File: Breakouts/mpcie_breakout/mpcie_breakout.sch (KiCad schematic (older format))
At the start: 28 parts, among them J1 9-39, J10 8-14,G, J2 1-9, J3 40-48,43-51, J4 PWR, J5 16-34, J6 USB, J7 SIM_Card, J8 USB_OTG, J9 APWR, U1 MPCIE-Socket

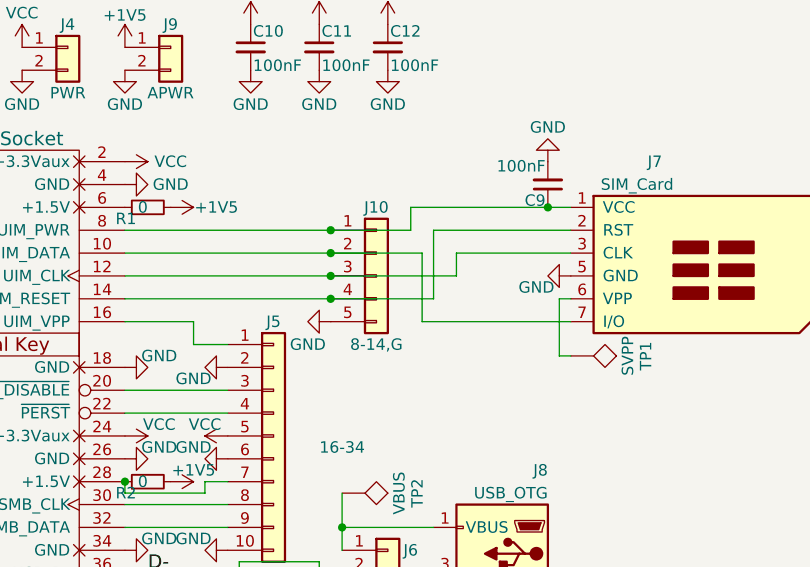
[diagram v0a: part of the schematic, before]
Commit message: Adding SIM net labels to mPCI-E breakout - SIM slot not fixed yet
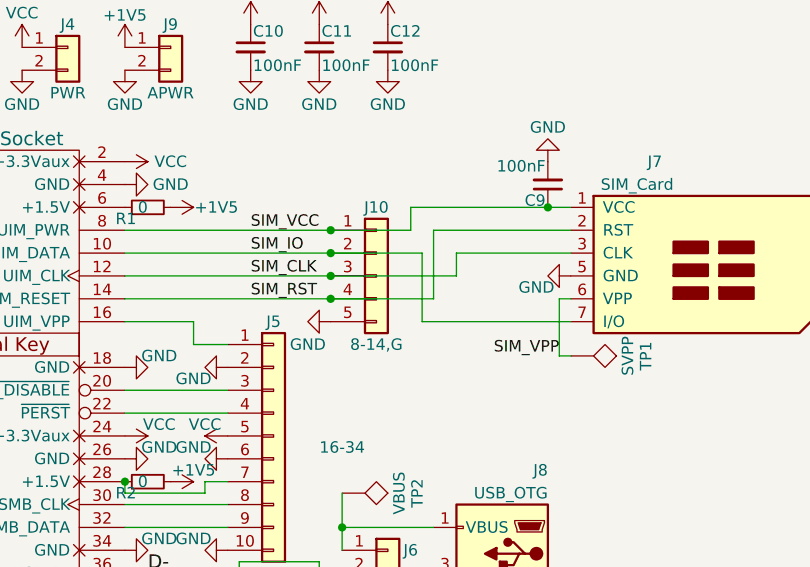
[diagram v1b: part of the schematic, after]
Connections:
- net SIM_IO: now reaches J10.2 (Pin_2), J7.7 (I/O), U1.10 (UIM_DATA)
- net SIM_CLK: now reaches J10.3 (Pin_3), J7.3 (CLK), U1.12 (UIM_CLK)
- net SIM_RST: now reaches J10.4 (Pin_4), J7.2 (RST), U1.14 (UIM_RESET)
- net SIM_VCC: now reaches C9.1, J10.1 (Pin_1), J7.1 (VCC), U1.8 (UIM_PWR)
- net SIM_VPP: now reaches J7.6 (VPP), TP1.1
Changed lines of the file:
@@
 Wire Wire Line
 	6150 2900 6600 2900
+Text Label 5800 2600 0    50   ~ 0
+SIM_VCC
+Text Label 5800 2700 0    50   ~ 0
+SIM_IO
+Text Label 5800 2800 0    50   ~ 0
+SIM_CLK
+Text Label 5800 2900 0    50   ~ 0
+SIM_RST
+Text Label 7150 3150 2    50   ~ 0
+SIM_VPP
 $EndSCHEMATC

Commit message: Adding v2 of the mPCIe breakout with a README
Changelog in README
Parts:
- added C13, C14: 100nF, Capacitor_SMD:C_0805_2012Metric, symbol Device:C_Small
- added U2: AP1117-33, Package_TO_SOT_SMD:SOT-223-3_TabPin2, symbol Regulator_Linear:AP1117-33
- added U3: AP1117-15, Package_TO_SOT_SMD:SOT-223-3_TabPin2, symbol Regulator_Linear:AP1117-15
- C1, C10, C11, C12, C2, C3, C4, C5, C6, C7, C8, C9: footprint Capacitors_SMD:C_0805 -> Capacitor_SMD:C_0805_2012Metric
- J1: symbol conn:Conn_01x16 -> mpcie_breakout-rescue:Conn_01x16-conn
- J10, J2, J6: symbol conn:Conn_01x05 -> mpcie_breakout-rescue:Conn_01x05-conn
- J3: symbol conn:Conn_02x05_Counter_Clockwise -> mpcie_breakout-rescue:Conn_02x05_Counter_Clockwise-conn
- J4, J9: symbol conn:Conn_01x02 -> mpcie_breakout-rescue:Conn_01x02-conn
- J5: symbol conn:Conn_01x10 -> mpcie_breakout-rescue:Conn_01x10-conn
- J7: symbol conn:SIM_Card -> mpcie_breakout-rescue:SIM_Card-conn
- J8: symbol conn:USB_OTG -> mpcie_breakout-rescue:USB_OTG-conn
- R1, R2, R3: footprint Resistors_SMD:R_0402 -> Resistor_SMD:R_0603_1608Metric_Pad1.05x0.95mm_HandSolder
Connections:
- net +1V5: now also U3.2 (VO)
- net GND: now also J7.C5 (GND), C13.2, C14.2, U2.1 (GND), U3.1 (GND); no longer J7.5 (GND)
- net SIM_CLK: now also J7.C3 (CLK); no longer J7.3 (CLK)
- net SIM_IO: now also J7.C7 (I/O); no longer J7.7 (I/O)
- net SIM_RST: now also J7.C2 (RST); no longer J7.2 (RST)
- net SIM_VCC: now also J7.C1 (VCC); no longer J7.1 (VCC)
- net SIM_VPP: now also J7.C6 (VPP); no longer J7.6 (VPP)
- net VCC: now also C13.1, U2.2 (VO)
- net VBUS: now reaches J6.1 (Pin_1), J8.1 (VBUS), TP2.1
- net VBUS: now also C14.1, U2.3 (VI), U3.3 (VI)
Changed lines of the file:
@@
 EESchema Schematic File Version 4
-LIBS:mpcie_breakout-cache
-EELAYER 29 0
+EELAYER 30 0
 EELAYER END
 $Descr A4 11693 8268
@@
 $EndComp
 $Comp
-L conn:SIM_Card J7
+L mpcie_breakout-rescue:SIM_Card-conn J7
 U 1 1 5CC07ACA
 P 7700 2800
@@
 $EndComp
 $Comp
-L conn:USB_OTG J8
+L mpcie_breakout-rescue:USB_OTG-conn J8
 U 1 1 5CC07C94
 P 6900 4100
@@
 F 0 "R1" V 5300 2550 50  0000 L CNN
 F 1 "0" V 5350 2500 50  0000 L CNN
-F 2 "Resistors_SMD:R_0402" H 5350 2500 50  0001 C CNN
+F 2 "Resistor_SMD:R_0603_1608Metric_Pad1.05x0.95mm_HandSolder" H 5350 2500 50  0001 C CNN
 F 3 "" H 5350 2500 50  0001 C CNN
 	1    5350 2500
@@
 F 0 "R3" V 5300 4750 50  0000 L CNN
 F 1 "0" V 5350 4700 50  0000 L CNN
-F 2 "Resistors_SMD:R_0402" H 5350 4700 50  0001 C CNN
+F 2 "Resistor_SMD:R_0603_1608Metric_Pad1.05x0.95mm_HandSolder" H 5350 4700 50  0001 C CNN
 F 3 "" H 5350 4700 50  0001 C CNN
 	1    5350 4700
@@
 $EndComp
 $Comp
-L conn:Conn_02x05_Counter_Clockwise J3
+L mpcie_breakout-rescue:Conn_02x05_Counter_Clockwise-conn J3
 U 1 1 5CC08111
 P 4600 5300
@@
 $EndComp
 $Comp
-L conn:Conn_01x05 J6
+L mpcie_breakout-rescue:Conn_01x05-conn J6
 U 1 1 5CC084A6
 P 6400 4200
@@
 $EndComp
 $Comp
-L conn:Conn_01x05 J2
+L mpcie_breakout-rescue:Conn_01x05-conn J2
 U 1 1 5CC08647
 P 3450 2500
@@
 $EndComp
 $Comp
-L conn:Conn_01x02 J4
+L mpcie_breakout-rescue:Conn_01x02-conn J4
 U 1 1 5CC088EB
 P 5000 1800
@@
 F 0 "R2" V 5300 3750 50  0000 L CNN
 F 1 "0" V 5350 3700 50  0000 L CNN
-F 2 "Resistors_SMD:R_0402" H 5350 3700 50  0001 C CNN
+F 2 "Resistor_SMD:R_0603_1608Metric_Pad1.05x0.95mm_HandSolder" H 5350 3700 50  0001 C CNN
 F 3 "" H 5350 3700 50  0001 C CNN
 	1    5350 3700
@@
 F 0 "C7" H 4010 1870 50  0000 L CNN
 F 1 "100nF" H 4010 1720 50  0000 L CNN
-F 2 "Capacitors_SMD:C_0805" H 4000 1800 50  0001 C CNN
+F 2 "Capacitor_SMD:C_0805_2012Metric" H 4000 1800 50  0001 C CNN
 F 3 "" H 4000 1800 50  0001 C CNN
 	1    4000 1800
@@
 F 0 "C8" H 4310 1870 50  0000 L CNN
 F 1 "100nF" H 4310 1720 50  0000 L CNN
-F 2 "Capacitors_SMD:C_0805" H 4300 1800 50  0001 C CNN
+F 2 "Capacitor_SMD:C_0805_2012Metric" H 4300 1800 50  0001 C CNN
 F 3 "" H 4300 1800 50  0001 C CNN
 	1    4300 1800
@@
 F 0 "C6" H 3710 1870 50  0000 L CNN
 F 1 "100nF" H 3710 1720 50  0000 L CNN
-F 2 "Capacitors_SMD:C_0805" H 3700 1800 50  0001 C CNN
+F 2 "Capacitor_SMD:C_0805_2012Metric" H 3700 1800 50  0001 C CNN
 F 3 "" H 3700 1800 50  0001 C CNN
 	1    3700 1800
@@
 F 0 "C5" H 3410 1870 50  0000 L CNN
 F 1 "100nF" H 3410 1720 50  0000 L CNN
-F 2 "Capacitors_SMD:C_0805" H 3400 1800 50  0001 C CNN
+F 2 "Capacitor_SMD:C_0805_2012Metric" H 3400 1800 50  0001 C CNN
 F 3 "" H 3400 1800 50  0001 C CNN
 	1    3400 1800
@@
 $EndComp
 $Comp
-L conn:Conn_01x16 J1
+L mpcie_breakout-rescue:Conn_01x16-conn J1
 U 1 1 5CC09A5E
 P 3100 3500
@@
 $EndComp
 $Comp
-L conn:Conn_01x10 J5
+L mpcie_breakout-rescue:Conn_01x10-conn J5
 U 1 1 5CC09F73
 P 5900 3500
 F 0 "J5" H 5900 4000 50  0000 C CNN
-F 1 "16-34" H 6200 3450 50  0000 C CNN
+F 1 "16-34" H 6100 3650 50  0000 C CNN
 F 2 "Pin_Headers:Pin_Header_Straight_2x05_Pitch2.54mm" H 5900 3500 50  0001 C CNN
 F 3 "" H 5900 3500 50  0001 C CNN
@@
 F 0 "C3" H 2860 1870 50  0000 L CNN
 F 1 "100nF" H 2860 1720 50  0000 L CNN
-F 2 "Capacitors_SMD:C_0805" H 2850 1800 50  0001 C CNN
+F 2 "Capacitor_SMD:C_0805_2012Metric" H 2850 1800 50  0001 C CNN
 F 3 "" H 2850 1800 50  0001 C CNN
 	1    2850 1800
@@
 F 0 "C4" H 3160 1870 50  0000 L CNN
 F 1 "100nF" H 3160 1720 50  0000 L CNN
-F 2 "Capacitors_SMD:C_0805" H 3150 1800 50  0001 C CNN
+F 2 "Capacitor_SMD:C_0805_2012Metric" H 3150 1800 50  0001 C CNN
 F 3 "" H 3150 1800 50  0001 C CNN
 	1    3150 1800
@@
 F 0 "C2" H 2560 1870 50  0000 L CNN
 F 1 "100nF" H 2560 1720 50  0000 L CNN
-F 2 "Capacitors_SMD:C_0805" H 2550 1800 50  0001 C CNN
+F 2 "Capacitor_SMD:C_0805_2012Metric" H 2550 1800 50  0001 C CNN
 F 3 "" H 2550 1800 50  0001 C CNN
 	1    2550 1800
@@
 F 0 "C1" H 2260 1870 50  0000 L CNN
 F 1 "100nF" H 2260 1720 50  0000 L CNN
-F 2 "Capacitors_SMD:C_0805" H 2250 1800 50  0001 C CNN
+F 2 "Capacitor_SMD:C_0805_2012Metric" H 2250 1800 50  0001 C CNN
 F 3 "" H 2250 1800 50  0001 C CNN
 	1    2250 1800
@@
 F 0 "C9" H 7110 2470 50  0000 L CNN
 F 1 "100nF" H 7110 2320 50  0000 L CNN
-F 2 "Capacitors_SMD:C_0805" H 7100 2400 50  0001 C CNN
+F 2 "Capacitor_SMD:C_0805_2012Metric" H 7100 2400 50  0001 C CNN
 F 3 "" H 7100 2400 50  0001 C CNN
 	1    7100 2400
@@
 $EndComp
 $Comp
-L conn:Conn_01x02 J9
+L mpcie_breakout-rescue:Conn_01x02-conn J9
 U 1 1 5CC0945A
 P 5450 1800
@@
 	6700 2800 6700 2700
 $Comp
-L conn:Conn_01x05 J10
+L mpcie_breakout-rescue:Conn_01x05-conn J10
 U 1 1 5CC0A195
 P 6350 2800
@@
 F 0 "C10" H 5810 1870 50  0000 L CNN
 F 1 "100nF" H 5810 1720 50  0000 L CNN
-F 2 "Capacitors_SMD:C_0805" H 5800 1800 50  0001 C CNN
+F 2 "Capacitor_SMD:C_0805_2012Metric" H 5800 1800 50  0001 C CNN
 F 3 "" H 5800 1800 50  0001 C CNN
 	1    5800 1800
@@
 F 0 "C11" H 6110 1870 50  0000 L CNN
 F 1 "100nF" H 6110 1720 50  0000 L CNN
-F 2 "Capacitors_SMD:C_0805" H 6100 1800 50  0001 C CNN
+F 2 "Capacitor_SMD:C_0805_2012Metric" H 6100 1800 50  0001 C CNN
 F 3 "" H 6100 1800 50  0001 C CNN
 	1    6100 1800
@@
 F 0 "C12" H 6410 1870 50  0000 L CNN
 F 1 "100nF" H 6410 1720 50  0000 L CNN
-F 2 "Capacitors_SMD:C_0805" H 6400 1800 50  0001 C CNN
+F 2 "Capacitor_SMD:C_0805_2012Metric" H 6400 1800 50  0001 C CNN
 F 3 "" H 6400 1800 50  0001 C CNN
 	1    6400 1800
@@
 Text Label 7150 3150 2    50   ~ 0
 SIM_VPP
+$Comp
+L Regulator_Linear:AP1117-33 U2
+U 1 1 5FF64EDB
+P 1300 3000
+F 0 "U2" H 1300 3242 50  0000 C CNN
+F 1 "AP1117-33" H 1300 3151 50  0000 C CNN
+F 2 "Package_TO_SOT_SMD:SOT-223-3_TabPin2" H 1300 3200 50  0001 C CNN
+F 3 "http://www.diodes.com/datasheets/AP1117.pdf" H 1400 2750 50  0001 C CNN
+	1    1300 3000
+	1    0    0    -1
+$EndComp
+$Comp
+L power:VBUS #PWR0101
+U 1 1 5FF67FCA
+P 6200 3750
+F 0 "#PWR0101" H 6200 3600 50  0001 C CNN
+F 1 "VBUS" H 6215 3923 50  0000 C CNN
+F 2 "" H 6200 3750 50  0001 C CNN
+F 3 "" H 6200 3750 50  0001 C CNN
+	1    6200 3750
+	1    0    0    -1
+$EndComp
+Connection ~ 6200 3750
+$Comp
+L power:VBUS #PWR0102
+U 1 1 5FF68DFF
+P 1000 3000
+F 0 "#PWR0102" H 1000 2850 50  0001 C CNN
+F 1 "VBUS" H 900 3150 50  0000 C CNN
+F 2 "" H 1000 3000 50  0001 C CNN
+F 3 "" H 1000 3000 50  0001 C CNN
+	1    1000 3000
+	1    0    0    -1
+$EndComp
+$Comp
+L power:VCC #PWR0103
+U 1 1 5FF6C4C8
+P 1600 3000
+F 0 "#PWR0103" H 1600 2850 50  0001 C CNN
+F 1 "VCC" H 1650 3150 50  0000 C CNN
+F 2 "" H 1600 3000 50  0001 C CNN
+F 3 "" H 1600 3000 50  0001 C CNN
+	1    1600 3000
+	1    0    0    -1
+$EndComp
+$Comp
+L power:GND #PWR0104
+U 1 1 5FF6E995
+P 1300 3300
+F 0 "#PWR0104" H 1300 3050 50  0001 C CNN
+F 1 "GND" H 1300 3150 50  0000 C CNN
+F 2 "" H 1300 3300 50  0001 C CNN
+F 3 "" H 1300 3300 50  0001 C CNN
+	1    1300 3300
+	1    0    0    -1
+$EndComp
+$Comp
+L Regulator_Linear:AP1117-15 U3
+U 1 1 5FF703B3
+P 1300 4100
+F 0 "U3" H 1300 4342 50  0000 C CNN
+F 1 "AP1117-15" H 1300 4251 50  0000 C CNN
+F 2 "Package_TO_SOT_SMD:SOT-223-3_TabPin2" H 1300 4300 50  0001 C CNN
+F 3 "http://www.diodes.com/datasheets/AP1117.pdf" H 1400 3850 50  0001 C CNN
+	1    1300 4100
+	1    0    0    -1
+$EndComp
+$Comp
+L power:VBUS #PWR0105
+U 1 1 5FF71952
+P 1000 4100
+F 0 "#PWR0105" H 1000 3950 50  0001 C CNN
+F 1 "VBUS" H 900 4250 50  0000 C CNN
+F 2 "" H 1000 4100 50  0001 C CNN
+F 3 "" H 1000 4100 50  0001 C CNN
+	1    1000 4100
+	1    0    0    -1
+$EndComp
+$Comp
+L power:+1V5 #PWR0106
+U 1 1 5FF721B1
+P 1600 4100
+F 0 "#PWR0106" H 1600 3950 50  0001 C CNN
+F 1 "+1V5" H 1600 4240 50  0000 C CNN
+F 2 "" H 1600 4100 50  0001 C CNN
+F 3 "" H 1600 4100 50  0001 C CNN
+	1    1600 4100
+	1    0    0    -1
+$EndComp
+$Comp
+L power:GND #PWR0107
+U 1 1 5FF729DE
+P 1300 4400
+F 0 "#PWR0107" H 1300 4150 50  0001 C CNN
+F 1 "GND" H 1300 4250 50  0000 C CNN
+F 2 "" H 1300 4400 50  0001 C CNN
+F 3 "" H 1300 4400 50  0001 C CNN
+	1    1300 4400
+	1    0    0    -1
+$EndComp
+$Comp
+L Device:C_Small C14
+U 1 1 5FF98EFD
+P 1450 5250
+F 0 "C14" H 1460 5320 50  0000 L CNN
+F 1 "100nF" H 1460 5170 50  0000 L CNN
+F 2 "Capacitor_SMD:C_0805_2012Metric" H 1450 5250 50  0001 C CNN
+F 3 "" H 1450 5250 50  0001 C CNN
+	1    1450 5250
+	1    0    0    -1
+$EndComp
+$Comp
+L Device:C_Small C13
+U 1 1 5FF98F03
+P 1150 5250
+F 0 "C13" H 1160 5320 50  0000 L CNN
+F 1 "100nF" H 1160 5170 50  0000 L CNN
+F 2 "Capacitor_SMD:C_0805_2012Metric" H 1150 5250 50  0001 C CNN
+F 3 "" H 1150 5250 50  0001 C CNN
+	1    1150 5250
+	1    0    0    -1
+$EndComp
+$Comp
+L power:VCC #PWR0108
+U 1 1 5FF98F09
+P 1150 5150
+F 0 "#PWR0108" H 1150 5000 50  0001 C CNN
+F 1 "VCC" H 1150 5300 50  0000 C CNN
+F 2 "" H 1150 5150 50  0001 C CNN
+F 3 "" H 1150 5150 50  0001 C CNN
+	1    1150 5150
+	1    0    0    -1
+$EndComp
+$Comp
+L power:GND #PWR0109
+U 1 1 5FF98F21
+P 1150 5350
+F 0 "#PWR0109" H 1150 5100 50  0001 C CNN
+F 1 "GND" H 1150 5200 50  0000 C CNN
+F 2 "" H 1150 5350 50  0001 C CNN
+F 3 "" H 1150 5350 50  0001 C CNN
+	1    1150 5350
+	1    0    0    -1
+$EndComp
+$Comp
+L power:GND #PWR0110
+U 1 1 5FF98F27
+P 1450 5350
+F 0 "#PWR0110" H 1450 5100 50  0001 C CNN
+F 1 "GND" H 1450 5200 50  0000 C CNN
+F 2 "" H 1450 5350 50  0001 C CNN
+F 3 "" H 1450 5350 50  0001 C CNN
+	1    1450 5350
+	1    0    0    -1
+$EndComp
+$Comp
+L power:VBUS #PWR0115
+U 1 1 5FF9F3D9
+P 1450 5150
+F 0 "#PWR0115" H 1450 5000 50  0001 C CNN
+F 1 "VBUS" H 1350 5300 50  0000 C CNN
+F 2 "" H 1450 5150 50  0001 C CNN
+F 3 "" H 1450 5150 50  0001 C CNN
+	1    1450 5150
+	1    0    0    -1
+$EndComp
 $EndSCHEMATC

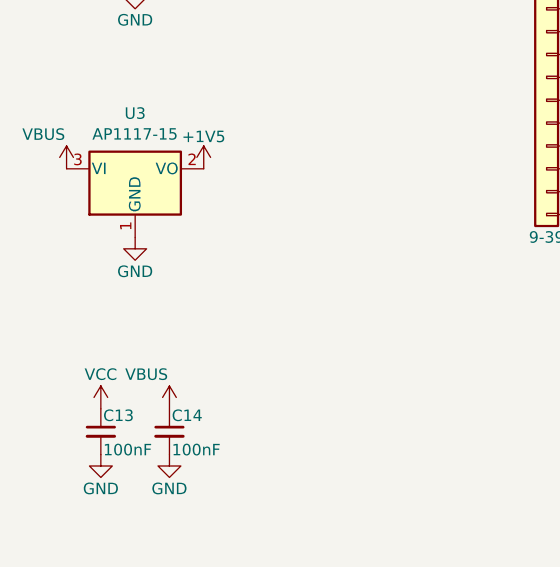
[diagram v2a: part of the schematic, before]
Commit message: Adding an ADJ resistor to the 1117-15 on the backside, rerouting diffpairs to decrease impedance a little bit
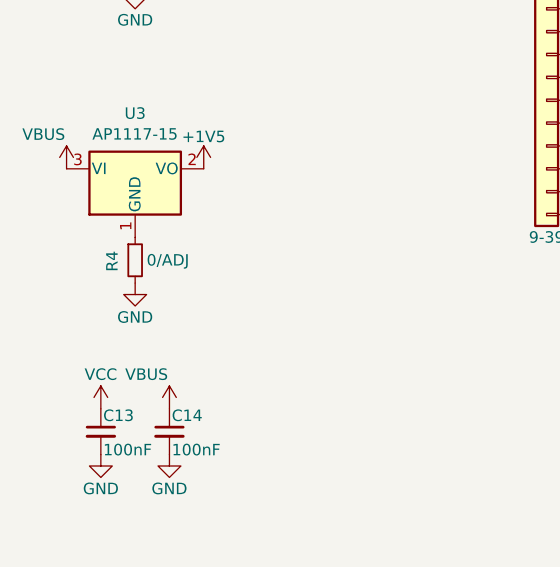
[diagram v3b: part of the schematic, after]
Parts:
- added R4: 0/ADJ, Resistor_SMD:R_0603_1608Metric_Pad0.98x0.95mm_HandSolder, symbol Device:R_Small
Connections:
- net GND: now also R4.2; no longer U3.1 (GND)
- new net: R4.1, U3.1 (GND)
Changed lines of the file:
@@
 L power:GND #PWR0107
 U 1 1 5FF729DE
-P 1300 4400
-F 0 "#PWR0107" H 1300 4150 50  0001 C CNN
-F 1 "GND" H 1300 4250 50  0000 C CNN
-F 2 "" H 1300 4400 50  0001 C CNN
-F 3 "" H 1300 4400 50  0001 C CNN
-	1    1300 4400
+P 1300 4600
+F 0 "#PWR0107" H 1300 4350 50  0001 C CNN
+F 1 "GND" H 1300 4450 50  0000 C CNN
+F 2 "" H 1300 4600 50  0001 C CNN
+F 3 "" H 1300 4600 50  0001 C CNN
+	1    1300 4600
 	1    0    0    -1
 $EndComp
@@
 	1    0    0    -1
 $EndComp
+$Comp
+L Device:R_Small R4
+U 1 1 618890E3
+P 1300 4500
+F 0 "R4" V 1200 4450 50  0000 L CNN
+F 1 "0/ADJ" H 1350 4500 50  0000 L CNN
+F 2 "Resistor_SMD:R_0603_1608Metric_Pad0.98x0.95mm_HandSolder" H 1300 4500 50  0001 C CNN
+F 3 "" H 1300 4500 50  0001 C CNN
+	1    1300 4500
+	1    0    0    -1
+$EndComp
